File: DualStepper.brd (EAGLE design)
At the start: 101.3 x 81.3 mm, 12 parts

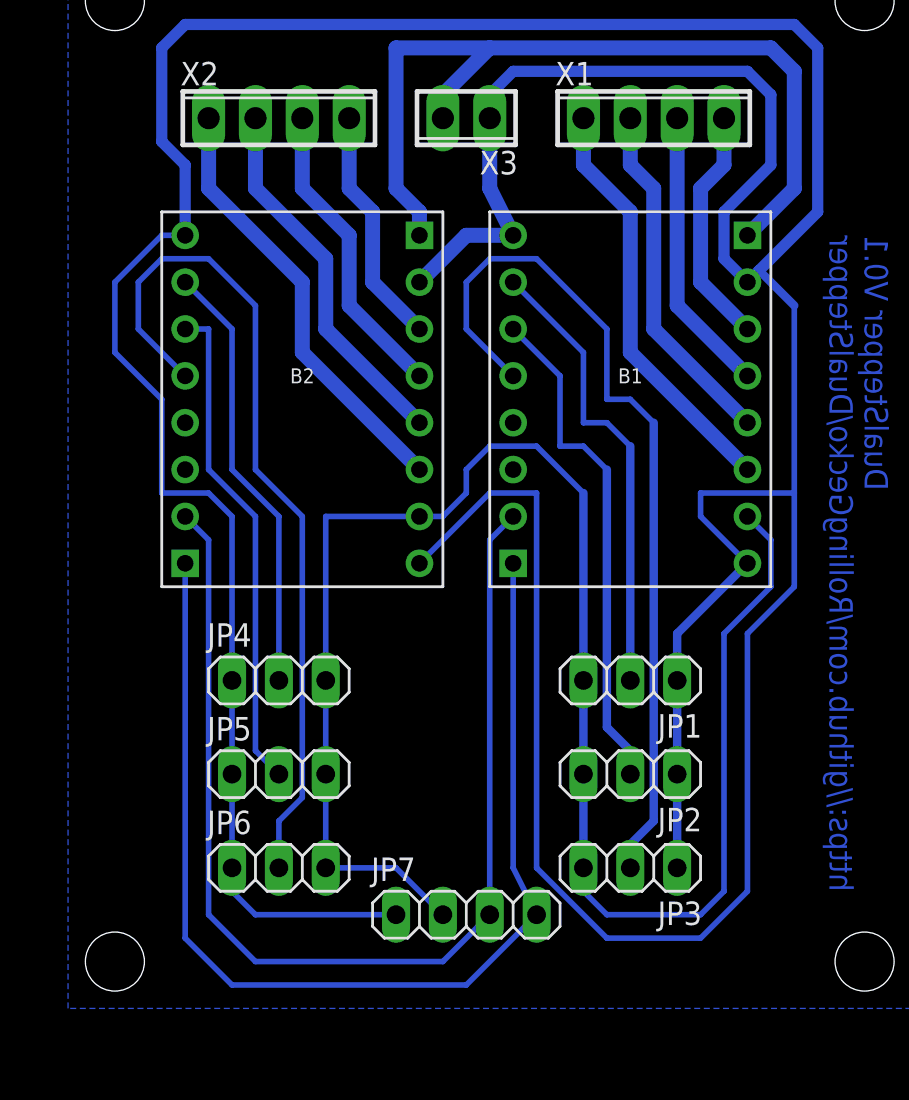
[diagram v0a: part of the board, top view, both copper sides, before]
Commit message: Final design with Phoenix conector to stepper and V+24V
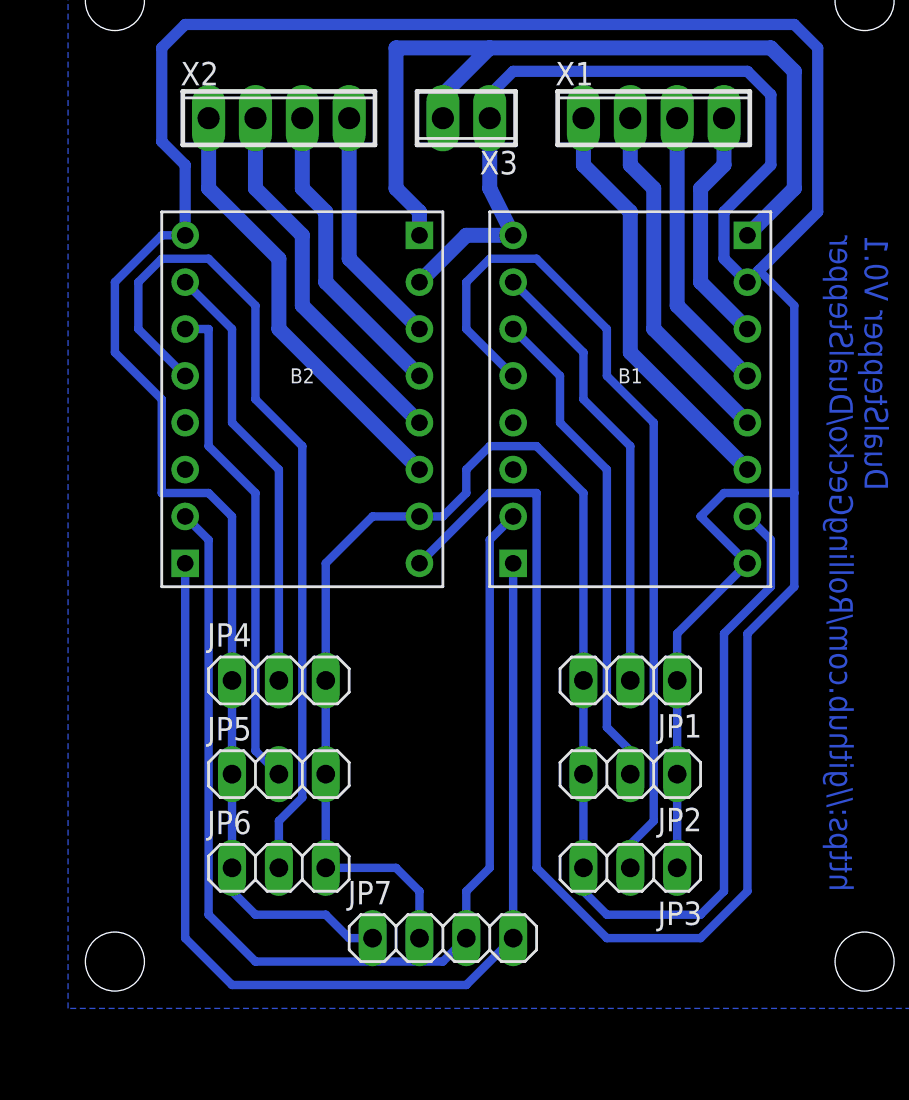
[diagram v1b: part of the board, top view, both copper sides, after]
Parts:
- moved JP7 1.80 mm to (45.7, 20.3)
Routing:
- net GND: track 260.9 -> 259.4 mm
- net N$15: track 61.4 -> 60.5 mm
- net +5V: track 106.1 -> 105.4 mm
- net N$14: track 25.0 -> 24.2 mm
- net N$12: track 27.5 -> 26.8 mm
- net N$13: track 47.4 -> 46.6 mm

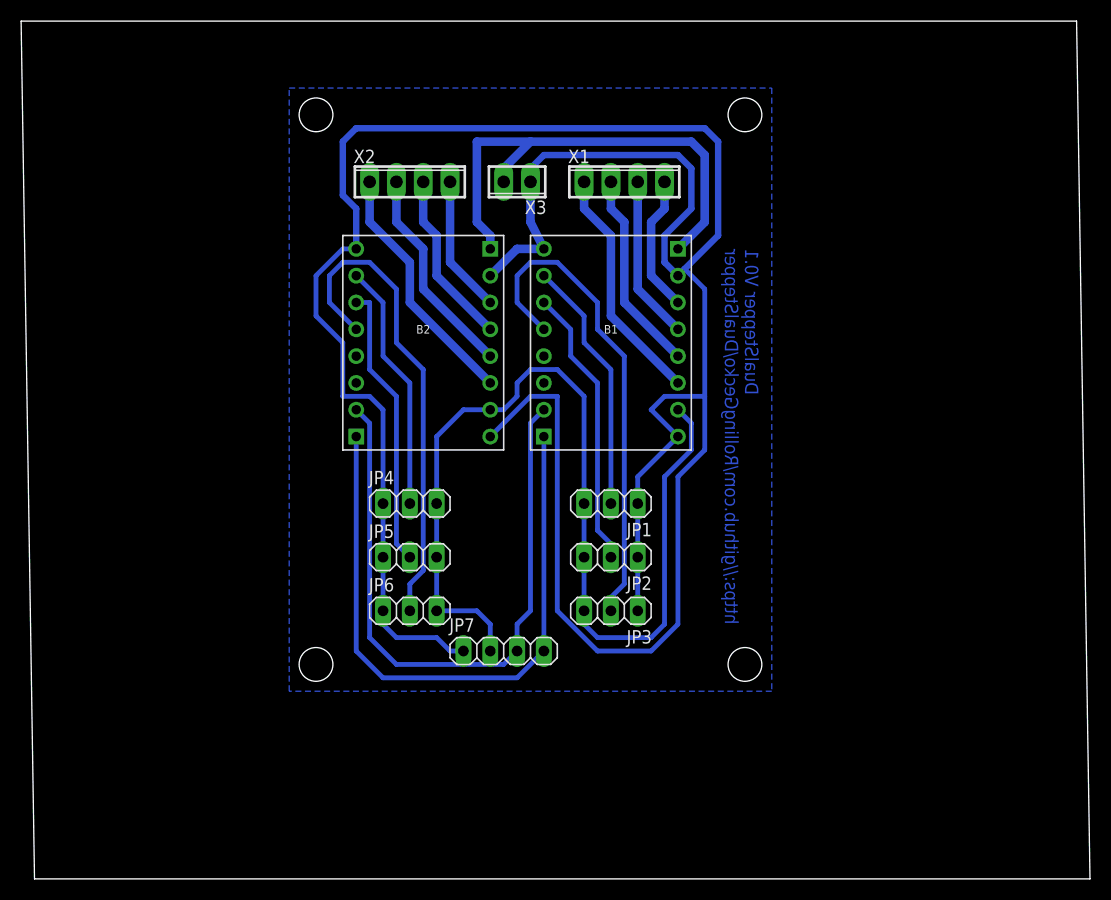
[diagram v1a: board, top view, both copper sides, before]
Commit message: Changed wire connectors to 5 mm grid
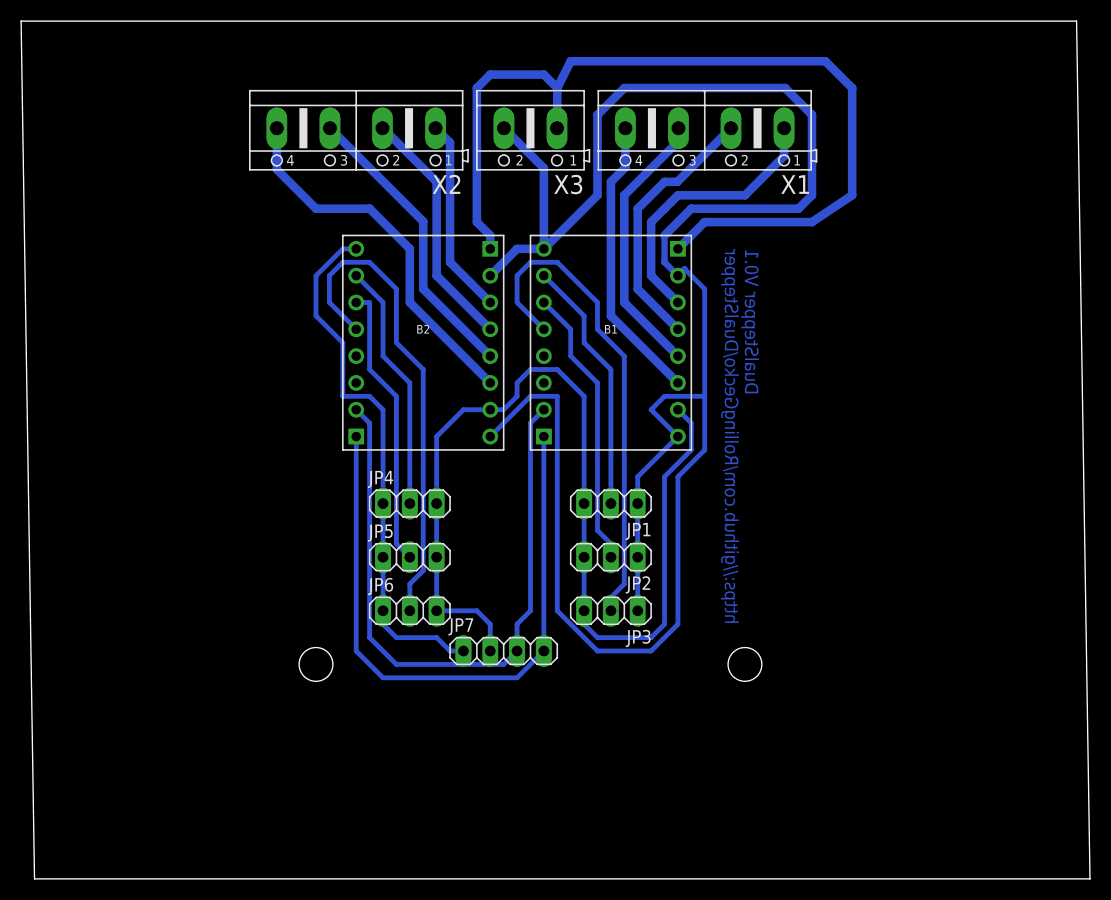
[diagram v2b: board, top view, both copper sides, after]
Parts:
- X1, X2: device con-phoenix-254:4POL254 -> con-ptr500:AK500/4
- X3: device con-phoenix-254:2POL254 -> con-ptr500:AK500/2
- moved X1 9.16 mm to (64.8, 69.8), turned to 180 degrees
- moved X2 7.18 mm to (31.8, 69.8), turned to 180 degrees
- moved X3 5.24 mm to (48.3, 69.8)
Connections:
- net +24V: now also X3.1; no longer X3.2
- net GND: now also X3.2; no longer X3.1
- net N$1: now also X1.1; no longer X1.4
- net N$2: now also X1.2; no longer X1.3
- net N$3: now also X1.3; no longer X1.2
- net N$4: now also X1.4; no longer X1.1
- net N$5: now also X2.4; no longer X2.1
- net N$6: now also X2.3; no longer X2.2
- net N$7: now also X2.2; no longer X2.3
- net N$8: now also X2.1; no longer X2.4
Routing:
- net +24V: track 47.6 -> 87.3 mm
- net GND: track 259.4 -> 240.5 mm
- net N$1: track 13.0 -> 26.5 mm
- net N$5: track 23.8 -> 35.5 mm
- net N$2: track 15.5 -> 25.0 mm
- net N$6: track 20.2 -> 27.9 mm
- net N$7: track 16.6 -> 23.3 mm
- net N$3: track 19.1 -> 25.8 mm
- net N$8: track 13.0 -> 18.7 mm
- net N$4: track 22.7 -> 27.3 mm
- removed copper zone on layer 16, net N$17

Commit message: Finael Version V0.1 for test
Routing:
- net GND: track 240.5 -> 272.2 mm
- net N$2: track 25.0 -> 29.4 mm
- net N$4: track 27.3 -> 31.7 mm
- net N$3: track 25.8 -> 29.8 mm
- net +24V: track 87.3 -> 83.4 mm
- net N$16: track 61.6 -> 64.4 mm
- net N$1: track 26.5 -> 29.2 mm
- net N$15: track 60.5 -> 63.0 mm
- added copper zone on layer 16, net N$17
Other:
- board text added: "DualStepper V0.1"
- board text added: "https://github.com/RollingGecko/DualStepper"
- board text removed: "DualStepper V0.1 https://github.com/RollingGecko/DualStepper"

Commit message: Eliminated one air wire
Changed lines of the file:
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@@
 <signal name="N$5">
 <contactref element="B2" pad="M1B"/>
-<wire x1="36.83" y1="58.42" x2="36.83" y2="53.34" width="0.8128" layer="16"/>
-<wire x1="36.83" y1="53.34" x2="44.45" y2="45.72" width="0.8128" layer="16"/>
 <contactref element="X2" pad="4"/>
-<wire x1="24.2316" y1="69.85" x2="44.45" y2="45.72" width="0" layer="19" extent="1-1"/>
-<wire x1="36.83" y1="58.42" x2="33.02" y2="62.23" width="0.8128" layer="16"/>
-<wire x1="24.2316" y1="69.85" x2="24.2316" y2="65.9384" width="0.8128" layer="16"/>
-<wire x1="24.2316" y1="65.9384" x2="27.94" y2="62.23" width="0.8128" layer="16"/>
-<wire x1="27.94" y1="62.23" x2="33.02" y2="62.23" width="0.8128" layer="16"/>
+<wire x1="24.2316" y1="69.85" x2="24.2316" y2="67.2324" width="0.8128" layer="16"/>
+<wire x1="24.2316" y1="67.2324" x2="29.5472" y2="67.2324" width="0.8128" layer="16"/>
+<wire x1="29.5472" y1="67.2324" x2="36.5584" y2="60.2212" width="0.8128" layer="16"/>
+<wire x1="36.5584" y1="60.2212" x2="36.5584" y2="53.9612" width="0.8128" layer="16"/>
+<wire x1="36.5584" y1="53.9612" x2="39.438" y2="51.0816" width="0.8128" layer="16"/>
+<wire x1="39.438" y1="51.0816" x2="39.438" y2="50.732" width="0.8128" layer="16"/>
+<wire x1="39.438" y1="50.732" x2="44.45" y2="45.72" width="0.8128" layer="16"/>
 </signal>
 <signal name="N$6">

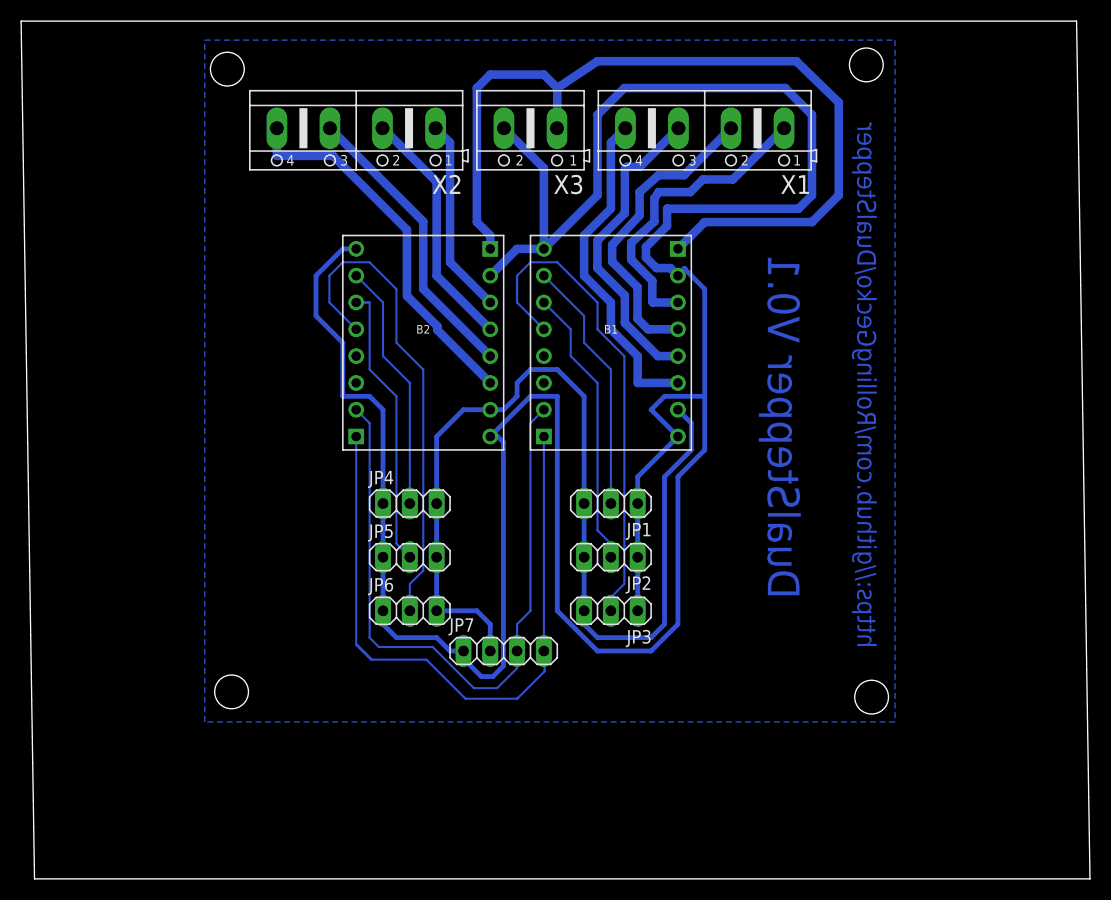
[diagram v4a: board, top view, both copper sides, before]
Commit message: Changed connectors to 3.5 RT
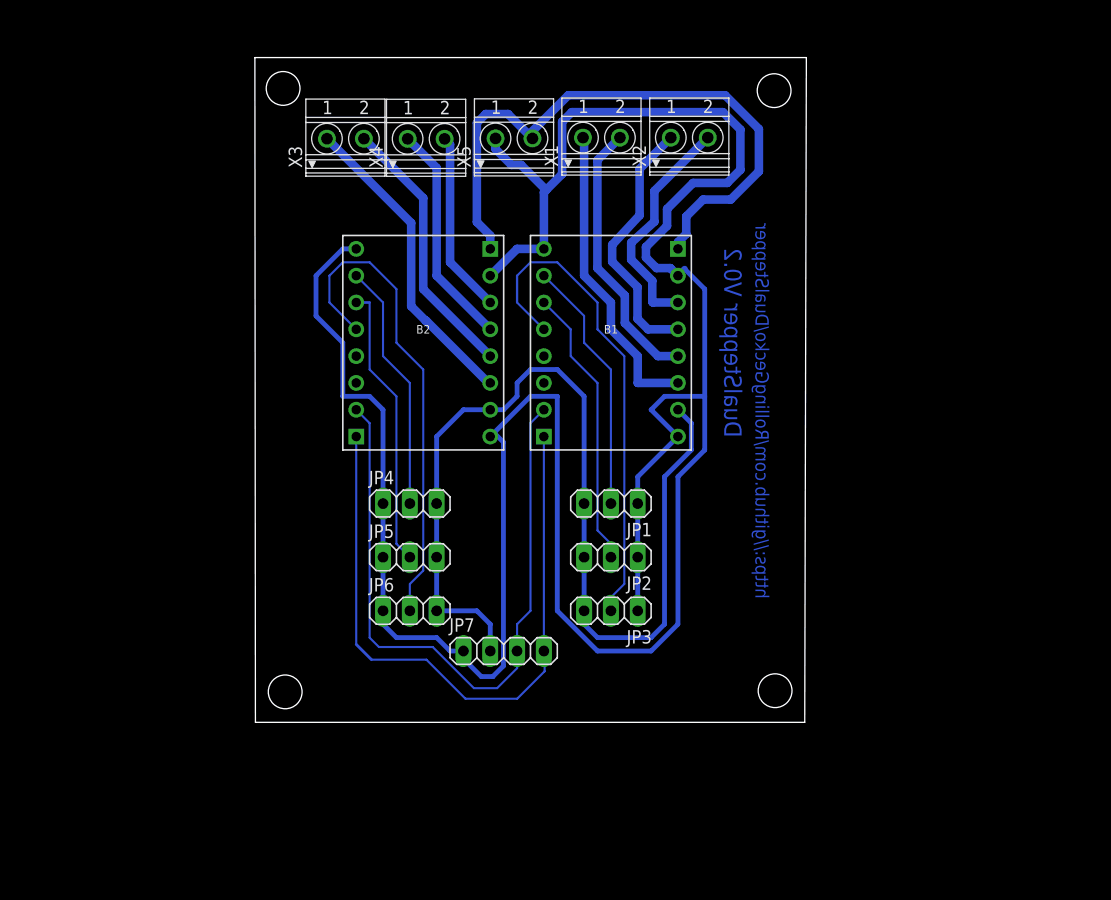
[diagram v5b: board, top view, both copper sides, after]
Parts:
- added X4, X5: 1751248, con-phoenix-350:1751248
- X1, X2: value (none) -> 1751248; device con-ptr500:AK500/4 -> con-phoenix-350:1751248
- X3: value (none) -> 1751248; device con-ptr500:AK500/2 -> con-phoenix-350:1751248
- moved X2 31.6 mm to (63.3, 69.1), turned to 0 degrees
- moved X3 17.6 mm to (30.7, 69.0), turned to 0 degrees
- moved X1 9.82 mm to (55.0, 69.1), turned to 0 degrees
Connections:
- net +24V: now also X5.2; no longer X3.1
- net GND: now also X5.1; no longer X3.2
- net N$1: now also X2.2; no longer X1.1
- net N$2: now also X2.1; no longer X1.2
- net N$3: now also X1.2; no longer X1.3
- net N$4: now also X1.1; no longer X1.4
- net N$5: now also X3.1; no longer X2.4
- net N$6: now also X3.2; no longer X2.3
- net N$7: now also X4.1; no longer X2.2
- net N$8: now also X4.2; no longer X2.1
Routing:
- net +24V: track 83.4 -> 59.8 mm
- net GND: track 272.2 -> 250.5 mm
- net N$1: track 29.2 -> 21.9 mm
- net N$5: track 35.6 -> 29.7 mm
- net N$2: track 29.4 -> 24.6 mm
- net N$3: track 29.8 -> 25.9 mm
- net N$4: track 31.7 -> 29.2 mm
- net N$6: track 27.9 -> 25.6 mm
- net N$7: track 23.3 -> 21.3 mm
- net N$8: track 18.7 -> 17.3 mm
- removed copper zone on layer 16, net N$17
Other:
- board size 101.3 x 81.3 mm -> 52.2 x 63 mm
- board text added: "DualStepper V0.2"
- board text removed: "DualStepper V0.1"

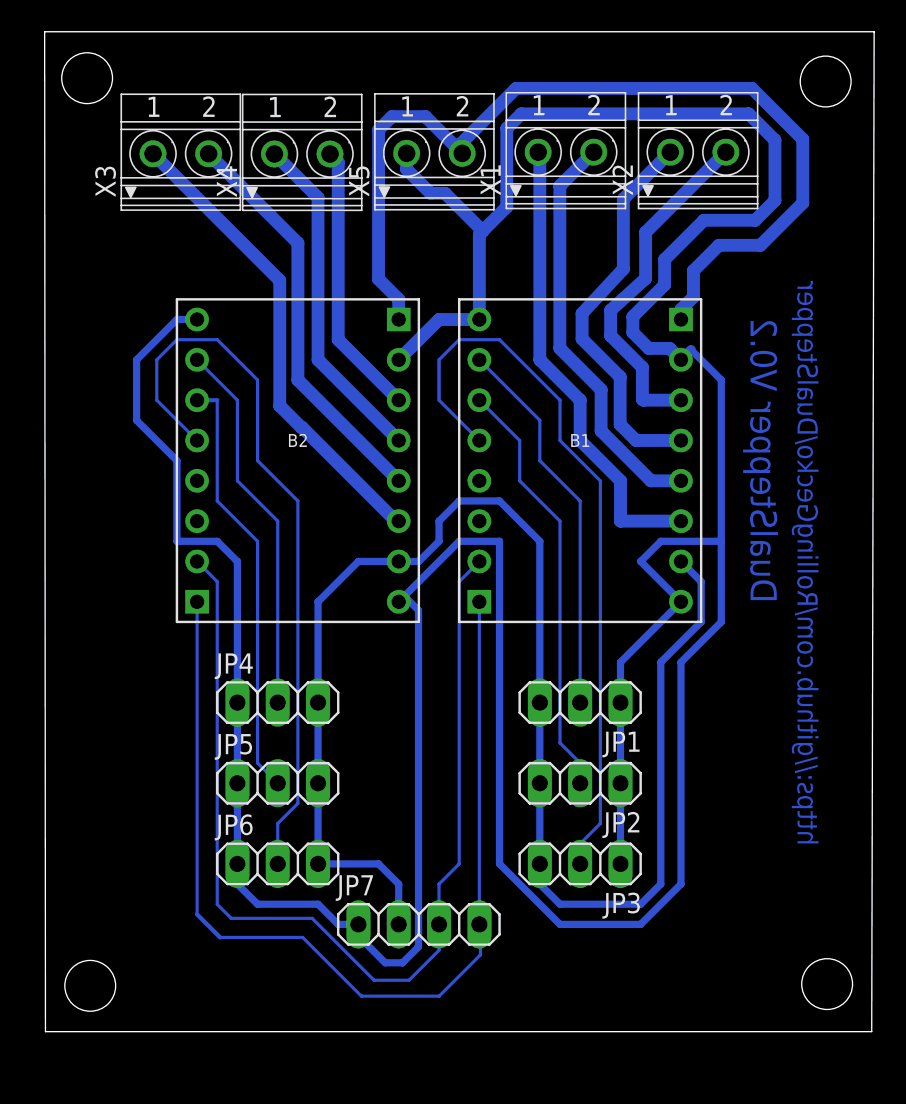
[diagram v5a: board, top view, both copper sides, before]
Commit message: Holes corrected
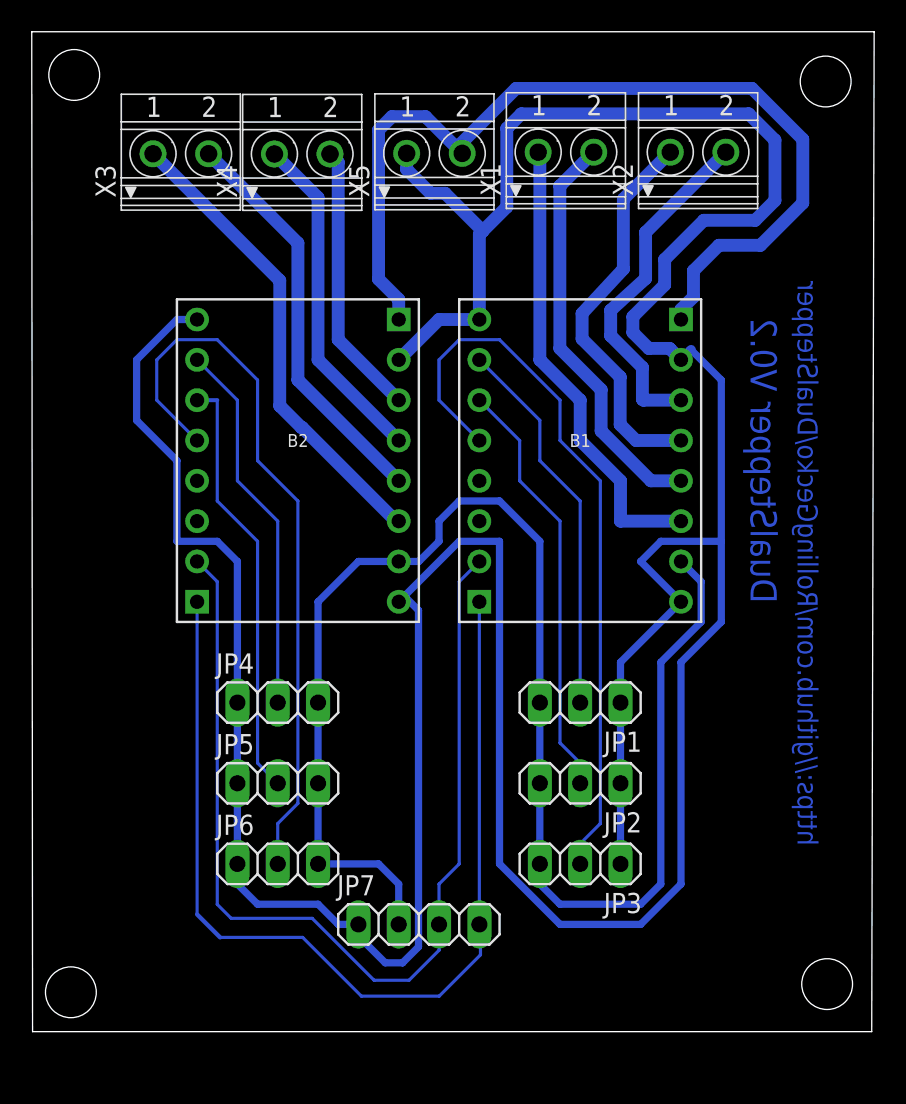
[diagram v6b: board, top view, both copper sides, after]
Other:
- board size 52.2 x 63 mm -> 53.1 x 63 mm
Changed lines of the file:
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@@
 <board>
 <plain>
-<wire x1="22.1996" y1="13.5636" x2="74.2444" y2="13.5636" width="0" layer="20"/>
+<wire x1="21.3868" y1="13.5636" x2="74.2444" y2="13.5636" width="0" layer="20"/>
 <wire x1="74.2444" y1="13.5636" x2="74.3968" y2="76.5456" width="0" layer="20"/>
-<wire x1="74.3968" y1="76.5456" x2="22.1488" y2="76.5456" width="0" layer="20"/>
-<wire x1="22.1488" y1="76.5456" x2="22.1996" y2="13.5636" width="0" layer="20"/>
+<wire x1="74.3968" y1="76.5456" x2="21.336" y2="76.5456" width="0" layer="20"/>
+<wire x1="21.336" y1="76.5456" x2="21.3868" y2="13.5636" width="0" layer="20"/>
 <text x="68.2636" y="58.5296" size="1.651" layer="16" rot="MR270">DualStepper V0.2</text>
-<hole x="25.02" y="16.45" drill="3.2"/>
+<hole x="23.8008" y="16.0436" drill="3.2"/>
 <hole x="71.436" y="16.5596" drill="3.2"/>
-<hole x="24.8232" y="73.6212" drill="3.2"/>
+<hole x="24.0104" y="73.8244" drill="3.2"/>
 <hole x="71.3424" y="73.4116" drill="3.2"/>
 <text x="70.84" y="60.8496" size="1.27" layer="16" rot="MR270"> https://github.com/RollingGecko/DualStepper</text>
